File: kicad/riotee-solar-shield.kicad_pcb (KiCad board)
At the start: 2 copper layers, 55.9 x 25.4 mm, 7 parts, among them J1 Conn_01x10, J2 Conn_01x12, SW1 SW_DIP_x02

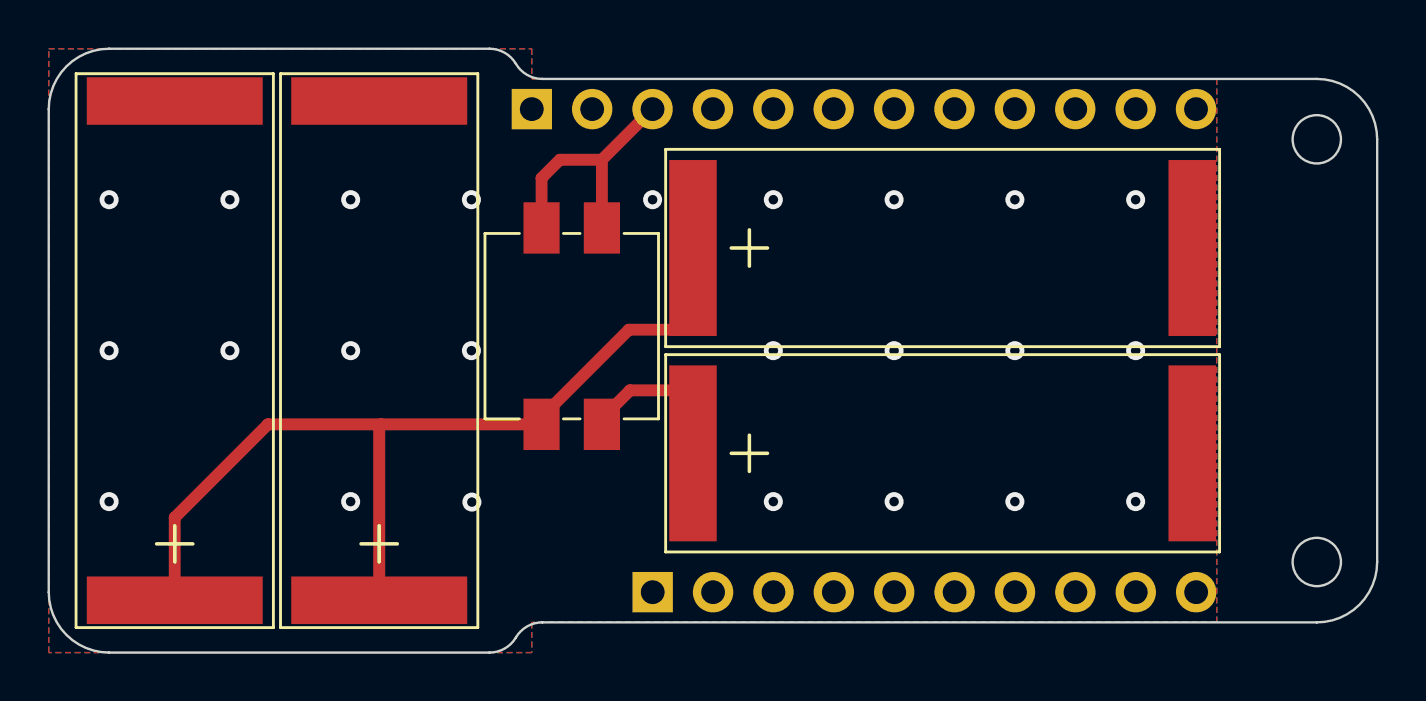
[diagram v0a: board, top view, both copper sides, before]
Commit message: add conformity marks and refine BOM
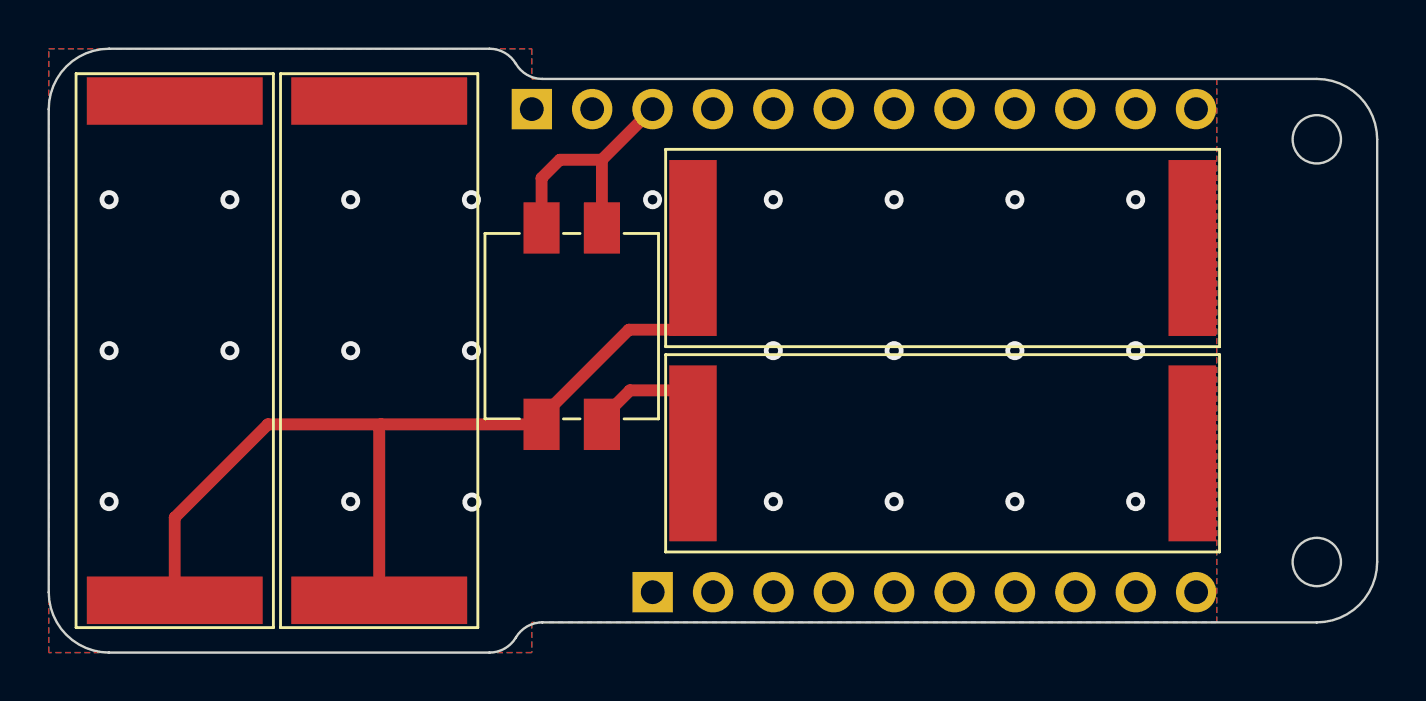
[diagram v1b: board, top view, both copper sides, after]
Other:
- board text added: "Riotee solar shield v1.0"
- board text removed: "Riotee solar shield v0.1"
